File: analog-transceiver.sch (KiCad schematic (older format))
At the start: 187 parts, among them J1 BNC, J2 AF In, J3 AF Out, Q1 2N3904, Q10 2N3904, Q11 2N3904, Q12 2N3904, Q13 2N3904, Q14 2N3904, Q15 2N3904, Q16 2N3904, Q17 2N3904, Q18 BF245A, Q19 2N3906, Q2 BF245A, Q20 2N3904, Q21 BF245A, Q22 2N7000, Q23 2N3904, Q24 2N3904, Q25 BD139, Q26 BD140, Q3 2N3904, Q4 2N3904, Q5 2N3906, Q6 2N3904, Q7 2N3904, Q8 2N3904, Q9 2N3904, Y1 10MHz, Y2 10MHz, Y3 10MHz, Y4 10MHz

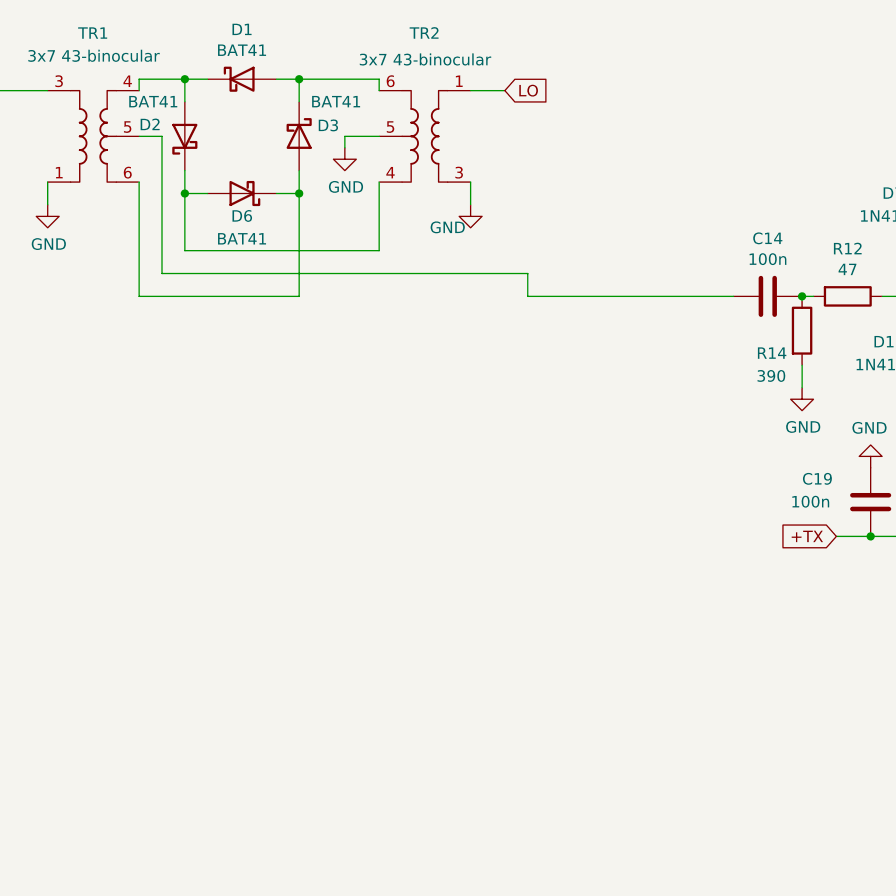
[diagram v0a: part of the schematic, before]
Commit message: Added Bridged Tee diplexer after diode DBM (10.7MHz@50ohms).
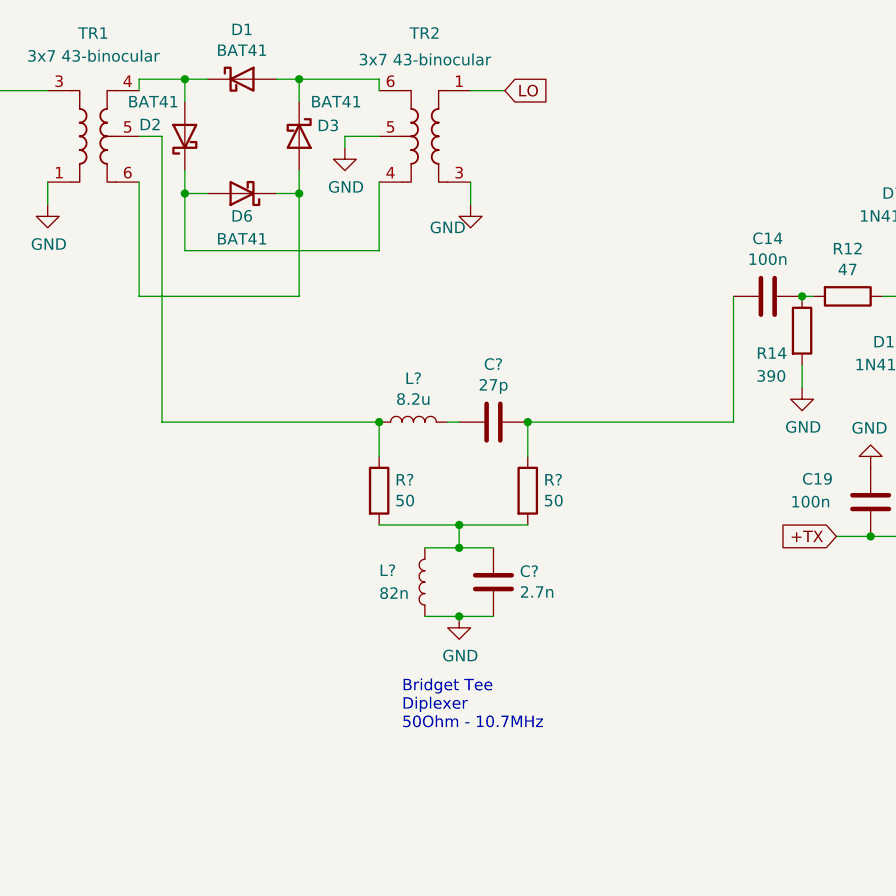
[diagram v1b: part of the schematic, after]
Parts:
- added C?: 2.7n, symbol Device:C
- added C?: 27p, symbol Device:C
- added L?: 82n, symbol Device:L
- added L?: 8.2u, symbol Device:L
- added R? (x2): 50, symbol Device:R
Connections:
- net GND: now also C?.2, L?.1
- net at TR1.5: now also L?.1, R?.1; no longer C14.2
- new net: C14.2, C?.1, R?.1
- new net: C?.1, L?.2, R?.2, R?.2
- new net: C?.2, L?.2
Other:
- note added: "Bridget Tee\nDiplexer\n50Ohm - 10.7MHz"
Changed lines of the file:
@@
 	6100 1850 6100 1800
 Wire Wire Line
-	4350 1850 5250 1850
-Wire Wire Line
 	6650 1300 7100 1300
 Connection ~ 7100 1300
@@
 Wire Wire Line
 	1900 950  2250 950
-Wire Wire Line
-	2750 1150 2750 1750
-Wire Wire Line
-	2750 1750 4350 1750
-Wire Wire Line
-	4350 1750 4350 1850
 $Comp
 L analog-transceiver-rescue:ADT1-1WT-Transformer TR6
@@
 Wire Wire Line
 	2750 9750 2450 9750
+$Comp
+L Device:R R?
+U 1 1 6357BA72
+P 3700 2700
+F 0 "R?" H 3770 2746 50  0000 L CNN
+F 1 "50" H 3770 2655 50  0000 L CNN
+F 2 "" V 3630 2700 50  0001 C CNN
+F 3 "~" H 3700 2700 50  0001 C CNN
+	1    3700 2700
+	1    0    0    -1
+$EndComp
+$Comp
+L Device:R R?
+U 1 1 6357D848
+P 4350 2700
+F 0 "R?" H 4420 2746 50  0000 L CNN
+F 1 "50" H 4420 2655 50  0000 L CNN
+F 2 "" V 4280 2700 50  0001 C CNN
+F 3 "~" H 4350 2700 50  0001 C CNN
+	1    4350 2700
+	1    0    0    -1
+$EndComp
+$Comp
+L Device:L L?
+U 1 1 6357F194
+P 3900 3100
+F 0 "L?" H 4100 3050 50  0000 R CNN
+F 1 "82n" H 4100 3150 50  0000 R CNN
+F 2 "" H 3900 3100 50  0001 C CNN
+F 3 "~" H 3900 3100 50  0001 C CNN
+	1    3900 3100
+	-1   0    0    1
+$EndComp
+$Comp
+L Device:L L?
+U 1 1 63581311
+P 3850 2400
+F 0 "L?" V 4040 2400 50  0000 C CNN
+F 1 "8.2u" V 3949 2400 50  0000 C CNN
+F 2 "" H 3850 2400 50  0001 C CNN
+F 3 "~" H 3850 2400 50  0001 C CNN
+	1    3850 2400
+	0    -1   -1   0
+$EndComp
+$Comp
+L Device:C C?
+U 1 1 63583747
+P 4200 3100
+F 0 "C?" H 4315 3146 50  0000 L CNN
+F 1 "2.7n" H 4315 3055 50  0000 L CNN
+F 2 "" H 4238 2950 50  0001 C CNN
+F 3 "~" H 4200 3100 50  0001 C CNN
+	1    4200 3100
+	1    0    0    -1
+$EndComp
+$Comp
+L Device:C C?
+U 1 1 63585ADB
+P 4200 2400
+F 0 "C?" V 3948 2400 50  0000 C CNN
+F 1 "27p" V 4039 2400 50  0000 C CNN
+F 2 "" H 4238 2250 50  0001 C CNN
+F 3 "~" H 4200 2400 50  0001 C CNN
+	1    4200 2400
+	0    1    1    0
+$EndComp
+$Comp
+L power:GND #PWR?
+U 1 1 635882C3
+P 4050 3250
+F 0 "#PWR?" H 4050 3000 50  0001 C CNN
+F 1 "GND" H 4055 3077 50  0000 C CNN
+F 2 "" H 4050 3250 50  0001 C CNN
+F 3 "" H 4050 3250 50  0001 C CNN
+	1    4050 3250
+	1    0    0    -1
+$EndComp
+Wire Wire Line
+	3900 2950 4050 2950
+Wire Wire Line
+	4200 3250 4050 3250
+Connection ~ 4050 3250
+Wire Wire Line
+	4050 3250 3900 3250
+Wire Wire Line
+	3700 2850 4050 2850
+Wire Wire Line
+	3700 2400 3700 2550
+Wire Wire Line
+	4000 2400 4050 2400
+Wire Wire Line
+	4350 2400 4350 2550
+Wire Wire Line
+	4050 2850 4050 2950
+Connection ~ 4050 2850
+Wire Wire Line
+	4050 2850 4350 2850
+Connection ~ 4050 2950
+Wire Wire Line
+	4050 2950 4200 2950
+Text Notes 3800 3750 0    50   ~ 0
+Bridget Tee\nDiplexer\n50Ohm - 10.7MHz
+Wire Wire Line
+	4350 2400 5250 2400
+Wire Wire Line
+	5250 2400 5250 1850
+Connection ~ 4350 2400
+Wire Wire Line
+	3700 2400 2750 2400
+Wire Wire Line
+	2750 1150 2750 2400
+Connection ~ 3700 2400
 $EndSCHEMATC
